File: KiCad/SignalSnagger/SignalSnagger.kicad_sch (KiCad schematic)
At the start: 81 parts, among them J101 Left, J102 Left, J103 Right, J104 Right, J105 36-5005-ND, J106 36-5006-ND, J107 36-5006-ND, J108 36-5005-ND, J909 36-5006-ND, J910 36-5006-ND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

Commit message: PCB Updates
31-Mar-2024
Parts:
- U102: value QS3253QG8 -> (none); footprint Package_SO:SSOP-16_3.9x4.9mm_P0.635mm -> (none)
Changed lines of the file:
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@@
       (effects (font (size 1.524 1.524) bold) (justify left))
     )
-    (property "Value" "QS3253QG8" (id 1) (at 210.82 45.72 0)
+    (property "Value" "" (id 1) (at 210.82 45.72 0)
       (effects (font (size 1.27 1.27) bold) (justify left))
     )
-    (property "Footprint" "Package_SO:SSOP-16_3.9x4.9mm_P0.635mm" (id 2) (at 199.39 54.61 0)
+    (property "Footprint" "" (id 2) (at 199.39 54.61 0)
       (effects (font (size 1.27 1.27)) hide)
     )
@@
     )
     (path "/2d0c2951-63ff-4560-b766-36e57ba946b0"
-      (reference "U102") (unit 1) (value "QS3253QG8") (footprint "Package_SO:SSOP-16_3.9x4.9mm_P0.635mm")
+      (reference "U102") (unit 1) (value "QS3253QG8") (footprint "Package_SO:SSOP-16_4.4x5.2mm_P0.65mm")
     )
     (path "/2fa45223-79ea-411b-839f-8bddbb1c8fec"

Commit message: Ver 0.315
BOM update
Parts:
- J102, J104: Digi-Key Part No. N/P -> SAM8996-ND; Manufacturer (none) -> Samtec Inc.; Manufacturer PN (none) -> TSW-104-07-F-D
- U102: value (none) -> QS3253QG8; footprint (none) -> Package_SO:SSOP-16_4.4x5.2mm_P0.65mm
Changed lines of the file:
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@@
   (title_block
     (title "SignalSnagger")
-    (date "2024-03-29")
-    (rev "0.314")
+    (date "2024-04-01")
+    (rev "0.315")
   )
   (junction (at 76.2 129.54) (diameter 0) (color 0 0 0 0)
@@
       (effects (font (size 1.524 1.524) bold) (justify left))
     )
-    (property "Value" "" (id 1) (at 210.82 45.72 0)
+    (property "Value" "QS3253QG8" (id 1) (at 210.82 45.72 0)
       (effects (font (size 1.27 1.27) bold) (justify left))
     )
-    (property "Footprint" "" (id 2) (at 199.39 54.61 0)
+    (property "Footprint" "Package_SO:SSOP-16_4.4x5.2mm_P0.65mm" (id 2) (at 199.39 54.61 0)
       (effects (font (size 1.27 1.27)) hide)
     )
@@
     (pin "1")
   )
-  (symbol (lib_id "Connector_Generic:Conn_02x04_Odd_Even") (at 68.58 92.71 0) (unit 1)
-    (in_bom yes) (on_board yes) (fields_autoplaced)
-    (property "Reference" "J104" (id 0) (at 69.85 85.2002 0))
-    (property "Value" "Right" (id 1) (at 69.85 87.7371 0))
-    (property "Footprint" "Connector_PinHeader_2.54mm:PinHeader_2x04_P2.54mm_Vertical" (id 2) (at 68.58 92.71 0)
-      (effects (font (size 1.27 1.27)) hide)
-    )
-    (property "Datasheet" "~" (id 3) (at 68.58 92.71 0)
-      (effects (font (size 1.27 1.27)) hide)
-    )
-    (property "Digi-Key Part No." "N/P" (id 4) (at 68.58 92.71 0)
-      (effects (font (size 1.27 1.27)) hide)
-    )
-    (pin "1")
-    (pin "2")
-    (pin "3")
-    (pin "4")
-    (pin "5")
-    (pin "6")
-    (pin "7")
-    (pin "8")
-  )
   (symbol (lib_id "Device:C_Trim_Small") (at 90.17 95.25 90) (mirror x) (unit 1)
     (in_bom yes) (on_board yes)
@@
       (effects (font (size 1.27 1.27)) hide)
     )
-    (property "Digi-Key Part No." "N/P" (id 4) (at 44.45 92.71 0)
+    (property "Digi-Key Part No." "SAM8996-ND" (id 4) (at 44.45 92.71 0)
+      (effects (font (size 1.27 1.27)) hide)
+    )
+    (property "Manufacturer" "Samtec Inc." (id 5) (at 44.45 92.71 0)
+      (effects (font (size 1.27 1.27)) hide)
+    )
+    (property "Manufacturer PN" "TSW-104-07-F-D" (id 6) (at 44.45 92.71 0)
+      (effects (font (size 1.27 1.27)) hide)
+    )
+    (property "Description" "CONN HEADER VERT 8POS 2.54MM" (id 7) (at 44.45 92.71 0)
       (effects (font (size 1.27 1.27)) hide)
     )
@@
     (pin "1")
   )
+  (symbol (lib_id "Connector_Generic:Conn_02x04_Odd_Even") (at 68.58 92.71 0) (unit 1)
+    (in_bom yes) (on_board yes) (fields_autoplaced)
+    (property "Reference" "J104" (id 0) (at 69.85 85.2002 0))
+    (property "Value" "Right" (id 1) (at 69.85 87.7371 0))
+    (property "Footprint" "Connector_PinHeader_2.54mm:PinHeader_2x04_P2.54mm_Vertical" (id 2) (at 68.58 92.71 0)
+      (effects (font (size 1.27 1.27)) hide)
+    )
+    (property "Datasheet" "~" (id 3) (at 68.58 92.71 0)
+      (effects (font (size 1.27 1.27)) hide)
+    )
+    (property "Digi-Key Part No." "SAM8996-ND" (id 4) (at 68.58 92.71 0)
+      (effects (font (size 1.27 1.27)) hide)
+    )
+    (property "Manufacturer" "Samtec Inc." (id 5) (at 68.58 92.71 0)
+      (effects (font (size 1.27 1.27)) hide)
+    )
+    (property "Manufacturer PN" "TSW-104-07-F-D" (id 6) (at 68.58 92.71 0)
+      (effects (font (size 1.27 1.27)) hide)
+    )
+    (property "Description" "CONN HEADER VERT 8POS 2.54MM" (id 7) (at 68.58 92.71 0)
+      (effects (font (size 1.27 1.27)) hide)
+    )
+    (pin "1")
+    (pin "2")
+    (pin "3")
+    (pin "4")
+    (pin "5")
+    (pin "6")
+    (pin "7")
+    (pin "8")
+  )
   (symbol (lib_id "Device:R_US") (at 139.7 180.34 0) (unit 1)
     (in_bom yes) (on_board yes)
@@
       (reference "J103") (unit 1) (value "Right") (footprint "Oddities:Dummy_Empty")
     )
-    (path "/331043fa-ab38-4872-afb0-dad5a0189da8"
+    (path "/edf6ad10-cc82-43d1-bc0a-205510d82ef2"
       (reference "J104") (unit 1) (value "Right") (footprint "Connector_PinHeader_2.54mm:PinHeader_2x04_P2.54mm_Vertical")
     )

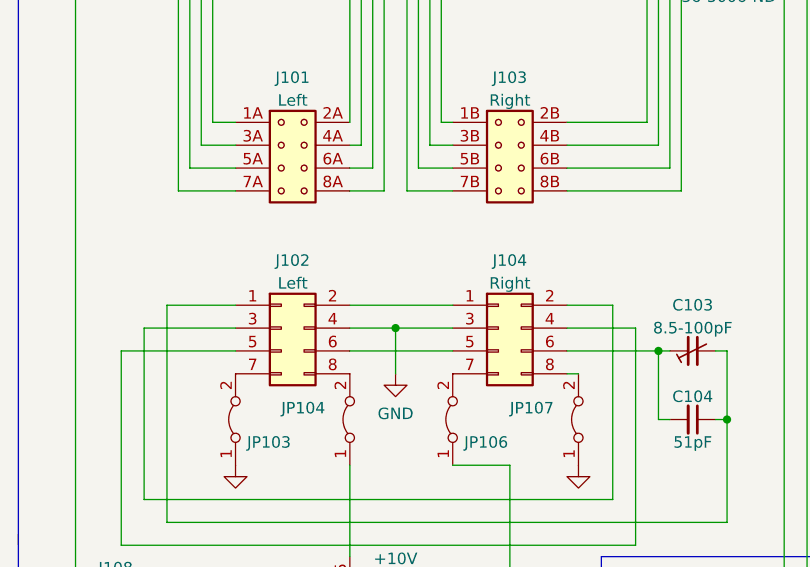
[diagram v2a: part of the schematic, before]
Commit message: PCB Updates
Moved programming header
Added ribbon cable plugs
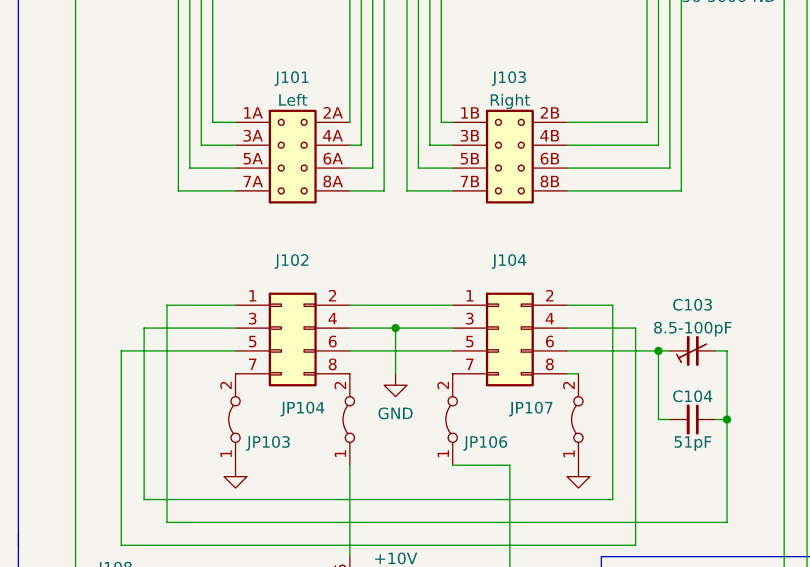
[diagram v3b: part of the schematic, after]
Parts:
- J102: value Left -> (none); footprint Connector_PinHeader_2.54mm:PinHeader_2x04_P2.54mm_Vertical -> (none); Digi-Key Part No. SAM8996-ND -> 609-3083-ND; Manufacturer Samtec Inc. -> Amphenol ICC (FCI); Manufacturer PN TSW-104-07-F-D -> 69830-008LF
- J104: value Right -> (none); footprint Connector_PinHeader_2.54mm:PinHeader_2x04_P2.54mm_Vertical -> (none); Digi-Key Part No. SAM8996-ND -> 609-3083-ND; Manufacturer Samtec Inc. -> Amphenol ICC (FCI); Manufacturer PN TSW-104-07-F-D -> 69830-008LF
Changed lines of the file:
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@@
     (pin "1")
+  )
+  (symbol (lib_id "Connector_Generic:Conn_02x04_Odd_Even") (at 68.58 92.71 0) (unit 1)
+    (in_bom yes) (on_board yes) (fields_autoplaced)
+    (property "Reference" "J104" (id 0) (at 69.85 85.2002 0))
+    (property "Value" "" (id 1) (at 69.85 87.7371 0))
+    (property "Footprint" "" (id 2) (at 68.58 92.71 0)
+      (effects (font (size 1.27 1.27)) hide)
+    )
+    (property "Datasheet" "~" (id 3) (at 68.58 92.71 0)
+      (effects (font (size 1.27 1.27)) hide)
+    )
+    (property "Digi-Key Part No." "609-3083-ND" (id 4) (at 68.58 92.71 0)
+      (effects (font (size 1.27 1.27)) hide)
+    )
+    (property "Manufacturer" "Amphenol ICC (FCI)" (id 5) (at 68.58 92.71 0)
+      (effects (font (size 1.27 1.27)) hide)
+    )
+    (property "Manufacturer PN" "69830-008LF" (id 6) (at 68.58 92.71 0)
+      (effects (font (size 1.27 1.27)) hide)
+    )
+    (property "Description" "CONN DIP HDR IDC 8POS VERT" (id 7) (at 68.58 92.71 0)
+      (effects (font (size 1.27 1.27)) hide)
+    )
+    (pin "1")
+    (pin "2")
+    (pin "3")
+    (pin "4")
+    (pin "5")
+    (pin "6")
+    (pin "7")
+    (pin "8")
   )
   (symbol (lib_id "Device:C_Small") (at 217.17 109.22 0) (unit 1)
@@
     (in_bom yes) (on_board yes) (fields_autoplaced)
     (property "Reference" "J102" (id 0) (at 45.72 85.2002 0))
-    (property "Value" "Left" (id 1) (at 45.72 87.7371 0))
-    (property "Footprint" "Connector_PinHeader_2.54mm:PinHeader_2x04_P2.54mm_Vertical" (id 2) (at 44.45 92.71 0)
+    (property "Value" "" (id 1) (at 45.72 87.7371 0))
+    (property "Footprint" "" (id 2) (at 44.45 92.71 0)
       (effects (font (size 1.27 1.27)) hide)
     )
@@
       (effects (font (size 1.27 1.27)) hide)
     )
-    (property "Digi-Key Part No." "SAM8996-ND" (id 4) (at 44.45 92.71 0)
-      (effects (font (size 1.27 1.27)) hide)
-    )
-    (property "Manufacturer" "Samtec Inc." (id 5) (at 44.45 92.71 0)
-      (effects (font (size 1.27 1.27)) hide)
-    )
-    (property "Manufacturer PN" "TSW-104-07-F-D" (id 6) (at 44.45 92.71 0)
-      (effects (font (size 1.27 1.27)) hide)
-    )
-    (property "Description" "CONN HEADER VERT 8POS 2.54MM" (id 7) (at 44.45 92.71 0)
+    (property "Digi-Key Part No." "609-3083-ND" (id 4) (at 44.45 92.71 0)
+      (effects (font (size 1.27 1.27)) hide)
+    )
+    (property "Manufacturer" "Amphenol ICC (FCI)" (id 5) (at 44.45 92.71 0)
+      (effects (font (size 1.27 1.27)) hide)
+    )
+    (property "Manufacturer PN" "69830-008LF" (id 6) (at 44.45 92.71 0)
+      (effects (font (size 1.27 1.27)) hide)
+    )
+    (property "Description" "CONN DIP HDR IDC 8POS VERT" (id 7) (at 44.45 92.71 0)
       (effects (font (size 1.27 1.27)) hide)
     )
@@
     (pin "1")
   )
-  (symbol (lib_id "Connector_Generic:Conn_02x04_Odd_Even") (at 68.58 92.71 0) (unit 1)
-    (in_bom yes) (on_board yes) (fields_autoplaced)
-    (property "Reference" "J104" (id 0) (at 69.85 85.2002 0))
-    (property "Value" "Right" (id 1) (at 69.85 87.7371 0))
-    (property "Footprint" "Connector_PinHeader_2.54mm:PinHeader_2x04_P2.54mm_Vertical" (id 2) (at 68.58 92.71 0)
-      (effects (font (size 1.27 1.27)) hide)
-    )
-    (property "Datasheet" "~" (id 3) (at 68.58 92.71 0)
-      (effects (font (size 1.27 1.27)) hide)
-    )
-    (property "Digi-Key Part No." "SAM8996-ND" (id 4) (at 68.58 92.71 0)
-      (effects (font (size 1.27 1.27)) hide)
-    )
-    (property "Manufacturer" "Samtec Inc." (id 5) (at 68.58 92.71 0)
-      (effects (font (size 1.27 1.27)) hide)
-    )
-    (property "Manufacturer PN" "TSW-104-07-F-D" (id 6) (at 68.58 92.71 0)
-      (effects (font (size 1.27 1.27)) hide)
-    )
-    (property "Description" "CONN HEADER VERT 8POS 2.54MM" (id 7) (at 68.58 92.71 0)
-      (effects (font (size 1.27 1.27)) hide)
-    )
-    (pin "1")
-    (pin "2")
-    (pin "3")
-    (pin "4")
-    (pin "5")
-    (pin "6")
-    (pin "7")
-    (pin "8")
-  )
   (symbol (lib_id "Device:R_US") (at 139.7 180.34 0) (unit 1)
     (in_bom yes) (on_board yes)
@@
     )
     (path "/90b403ba-135c-4ead-befc-3bc52036bd7e"
-      (reference "J102") (unit 1) (value "Left") (footprint "Connector_PinHeader_2.54mm:PinHeader_2x04_P2.54mm_Vertical")
+      (reference "J102") (unit 1) (value "Left") (footprint "Connector_Amphenol:69830-008LF")
     )
     (path "/b7c2c456-0540-49da-b4e7-60791f157ca9"
       (reference "J103") (unit 1) (value "Right") (footprint "Oddities:Dummy_Empty")
     )
-    (path "/edf6ad10-cc82-43d1-bc0a-205510d82ef2"
-      (reference "J104") (unit 1) (value "Right") (footprint "Connector_PinHeader_2.54mm:PinHeader_2x04_P2.54mm_Vertical")
+    (path "/8cd502e3-a78c-4b2f-8c7f-c0f8cafe4ad6"
+      (reference "J104") (unit 1) (value "Right") (footprint "Connector_Amphenol:69830-008LF")
     )
     (path "/1827fd48-a0ad-4504-ad60-021c20fdb5f0"

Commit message: PCB Layout
Most 3D models have been included in the schematic
PCB layout places all tall parts on the back of the board
Added knob to BOM
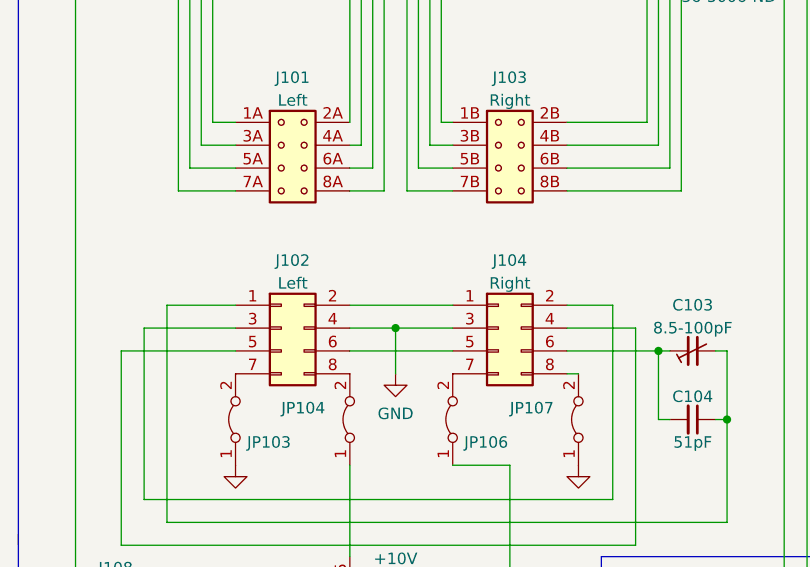
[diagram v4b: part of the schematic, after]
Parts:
- J102: value (none) -> Left; footprint (none) -> Connector_Amphenol:69830-008LF
- J104: value (none) -> Right; footprint (none) -> Connector_Amphenol:69830-008LF
- RV101: footprint Potentiometer_THT:Bourns_PV36W_Multiturn_Pot -> Potentiometer_THT:Potentiometer_Bourns_3362P_Vertical
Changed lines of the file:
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@@
   (title_block
     (title "SignalSnagger")
-    (date "2024-04-01")
-    (rev "0.315")
+    (date "2024-04-11")
+    (rev "0.316")
   )
   (junction (at 76.2 129.54) (diameter 0) (color 0 0 0 0)
@@
     (in_bom yes) (on_board yes) (fields_autoplaced)
     (property "Reference" "J104" (id 0) (at 69.85 85.2002 0))
-    (property "Value" "" (id 1) (at 69.85 87.7371 0))
-    (property "Footprint" "" (id 2) (at 68.58 92.71 0)
+    (property "Value" "Right" (id 1) (at 69.85 87.7371 0))
+    (property "Footprint" "Connector_Amphenol:69830-008LF" (id 2) (at 68.58 92.71 0)
       (effects (font (size 1.27 1.27)) hide)
     )
@@
     (in_bom yes) (on_board yes) (fields_autoplaced)
     (property "Reference" "J102" (id 0) (at 45.72 85.2002 0))
-    (property "Value" "" (id 1) (at 45.72 87.7371 0))
-    (property "Footprint" "" (id 2) (at 44.45 92.71 0)
+    (property "Value" "Left" (id 1) (at 45.72 87.7371 0))
+    (property "Footprint" "Connector_Amphenol:69830-008LF" (id 2) (at 44.45 92.71 0)
       (effects (font (size 1.27 1.27)) hide)
     )
@@
     (property "Reference" "RV101" (id 0) (at 33.02 133.35 90))
     (property "Value" "10k 10T" (id 1) (at 36.83 140.97 90))
-    (property "Footprint" "Potentiometer_THT:Bourns_PV36W_Multiturn_Pot" (id 2) (at 34.29 140.97 0)
+    (property "Footprint" "Potentiometer_THT:Potentiometer_Bourns_3362P_Vertical" (id 2) (at 34.29 140.97 0)
       (effects (font (size 1.27 1.27)) hide)
     )
@@
       (reference "JP301") (unit 1) (value "SolderJumper_2_Open") (footprint "Jumper:SolderJumper-2_P1.3mm_Open_RoundedPad1.0x1.5mm")
     )
+    (path "/a07b7207-b2ba-4964-b1bd-fe9eb7be7391/3433a5ee-7118-4568-bf67-046adea068c5"
+      (reference "Knob401") (unit 1) (value "Logo_Open_Hardware_Small") (footprint "")
+    )
     (path "/b7e6c0d8-791a-469a-85d5-f8e886443224/baca905f-d9c0-4905-a617-69cf46299e1f"
       (reference "L201") (unit 1) (value "10uH") (footprint "Inductor_SMD:L_0603_1608Metric")
@@
     )
     (path "/c0687338-f6ed-4456-aad9-d29c3bd35909"
-      (reference "RV101") (unit 1) (value "10k 10T") (footprint "Potentiometer_THT:Bourns_PV36W_Multiturn_Pot")
+      (reference "RV101") (unit 1) (value "10k 10T") (footprint "Potentiometer_THT:Potentiometer_Bourns_3362P_Vertical")
     )
     (path "/22206298-fd84-4e61-b115-2fa251b44661"

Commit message: Ver 0.317
PCB Tweaks
FreeCAD model updates
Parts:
- RV101: Digi-Key Part No. 118-PV36W103C01B00-ND -> 3362P-103LF-ND; Link https://www.digikey.com/en/products/detail/bourns-inc/PV36W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 -> https://www.digikey.com/en/products/detail/bourns-inc/3362P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; Manufacturer PN PV36W103C01B00 -> 3362P-1-103LF
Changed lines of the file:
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@@
   (title_block
     (title "SignalSnagger")
-    (date "2024-04-11")
-    (rev "0.316")
+    (date "2024-04-13")
+    (rev "0.317")
   )
   (junction (at 76.2 129.54) (diameter 0) (color 0 0 0 0)
@@
       (effects (font (size 1.27 1.27)) hide)
     )
-    (property "Digi-Key Part No." "118-PV36W103C01B00-ND" (id 4) (at 34.29 140.97 0)
+    (property "Digi-Key Part No." "3362P-103LF-ND" (id 4) (at 34.29 140.97 0)
       (effects (font (size 1.27 1.27)) hide)
     )
-    (property "Link" "https://www.digikey.com/en/products/detail/bourns-inc/PV36W103C01B00/666502?s=N4IgTCBcDaIAoDUDMA2A6gRgAxIMJYwCEssQBdAXyA" (id 5) (at 34.29 140.97 0)
+    (property "Link" "https://www.digikey.com/en/products/detail/bourns-inc/3362P-1-103LF/1088412?s=N4IgTCBcDaIMxwGxgAoFoCMAGOAZAYmgHIAiIAugL5A" (id 5) (at 34.29 140.97 0)
       (effects (font (size 1.27 1.27)) hide)
     )
@@
       (effects (font (size 1.27 1.27)) hide)
     )
-    (property "Manufacturer PN" "PV36W103C01B00" (id 7) (at 34.29 140.97 0)
+    (property "Manufacturer PN" "3362P-1-103LF" (id 7) (at 34.29 140.97 0)
       (effects (font (size 1.27 1.27)) hide)
     )
-    (property "Description" "10 kOhms 0.5W, 1/2W PC Pins Through Hole Trimmer Potentiometer Cermet 25 Turn Top Adjustment" (id 8) (at 34.29 140.97 0)
+    (property "Description" "TRIMMER 10K OHM 0.5W PC PIN TOP" (id 8) (at 34.29 140.97 0)
       (effects (font (size 1.27 1.27)) hide)
     )

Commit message: BOM Updates
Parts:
- J102: value Left -> (none); footprint Connector_Amphenol:69830-008LF -> (none)
- J104: value Right -> (none); footprint Connector_Amphenol:69830-008LF -> (none)
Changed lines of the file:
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@@
-    (pin "1")
-  )
-  (symbol (lib_id "Connector_Generic:Conn_01x01") (at 96.52 52.07 0) (unit 1)
-    (in_bom yes) (on_board yes)
-    (property "Reference" "J106" (id 0) (at 95.25 49.53 0)
-      (effects (font (size 1.27 1.27)) (justify left))
-    )
-    (property "Value" "36-5006-ND" (id 1) (at 88.9 55.88 0)
-      (effects (font (size 1.27 1.27)) (justify left))
-    )
-    (property "Footprint" "Connector_Pin:Pin_D1.6mm_L8.5mm_W2.8mm_FlatFork" (id 2) (at 96.52 52.07 0)
-      (effects (font (size 1.27 1.27)) hide)
-    )
-    (property "Datasheet" "~" (id 3) (at 96.52 52.07 0)
-      (effects (font (size 1.27 1.27)) hide)
-    )
-    (property "Digi-Key Part No." "N/P" (id 4) (at 96.52 52.07 0)
-      (effects (font (size 1.27 1.27)) hide)
-    )
     (pin "1")
   )
   (symbol (lib_id "Connector_Generic:Conn_02x04_Odd_Even") (at 68.58 92.71 0) (unit 1)
     (in_bom yes) (on_board yes) (fields_autoplaced)
-    (property "Reference" "J104" (id 0) (at 69.85 85.2002 0))
-    (property "Value" "Right" (id 1) (at 69.85 87.7371 0))
-    (property "Footprint" "Connector_Amphenol:69830-008LF" (id 2) (at 68.58 92.71 0)
+    (property "Reference" "J104" (id 0) (at 69.85 87.7372 0))
+    (property "Value" "" (id 1) (at 69.85 87.7371 0)
+      (effects (font (size 1.27 1.27)) hide)
+    )
+    (property "Footprint" "" (id 2) (at 68.58 92.71 0)
       (effects (font (size 1.27 1.27)) hide)
     )
@@
     (pin "8")
   )
+  (symbol (lib_id "Connector_Generic:Conn_01x01") (at 96.52 52.07 0) (unit 1)
+    (in_bom yes) (on_board yes)
+    (property "Reference" "J106" (id 0) (at 95.25 49.53 0)
+      (effects (font (size 1.27 1.27)) (justify left))
+    )
+    (property "Value" "36-5006-ND" (id 1) (at 88.9 55.88 0)
+      (effects (font (size 1.27 1.27)) (justify left))
+    )
+    (property "Footprint" "Connector_Pin:Pin_D1.6mm_L8.5mm_W2.8mm_FlatFork" (id 2) (at 96.52 52.07 0)
+      (effects (font (size 1.27 1.27)) hide)
+    )
+    (property "Datasheet" "~" (id 3) (at 96.52 52.07 0)
+      (effects (font (size 1.27 1.27)) hide)
+    )
+    (property "Digi-Key Part No." "N/P" (id 4) (at 96.52 52.07 0)
+      (effects (font (size 1.27 1.27)) hide)
+    )
+    (pin "1")
+  )
   (symbol (lib_id "Device:C_Small") (at 217.17 109.22 0) (unit 1)
     (in_bom yes) (on_board yes)
@@
   (symbol (lib_id "Connector_Generic:Conn_02x04_Odd_Even") (at 44.45 92.71 0) (unit 1)
     (in_bom yes) (on_board yes) (fields_autoplaced)
-    (property "Reference" "J102" (id 0) (at 45.72 85.2002 0))
-    (property "Value" "Left" (id 1) (at 45.72 87.7371 0))
-    (property "Footprint" "Connector_Amphenol:69830-008LF" (id 2) (at 44.45 92.71 0)
+    (property "Reference" "J102" (id 0) (at 45.72 87.7372 0))
+    (property "Value" "" (id 1) (at 45.72 87.7371 0)
+      (effects (font (size 1.27 1.27)) hide)
+    )
+    (property "Footprint" "" (id 2) (at 44.45 92.71 0)
       (effects (font (size 1.27 1.27)) hide)
     )
@@
     )
     (path "/90b403ba-135c-4ead-befc-3bc52036bd7e"
-      (reference "J102") (unit 1) (value "Left") (footprint "Connector_Amphenol:69830-008LF")
+      (reference "J102") (unit 1) (value "69830-008LF") (footprint "Connector_Amphenol:69830-008LF")
     )
     (path "/b7c2c456-0540-49da-b4e7-60791f157ca9"
       (reference "J103") (unit 1) (value "Right") (footprint "Oddities:Dummy_Empty")
     )
-    (path "/8cd502e3-a78c-4b2f-8c7f-c0f8cafe4ad6"
-      (reference "J104") (unit 1) (value "Right") (footprint "Connector_Amphenol:69830-008LF")
+    (path "/8a0e5179-fef2-43e1-bcf9-390e85dd7c99"
+      (reference "J104") (unit 1) (value "69830-008LF") (footprint "Connector_Amphenol:69830-008LF")
     )
     (path "/1827fd48-a0ad-4504-ad60-021c20fdb5f0"
@@
       (reference "U205") (unit 1) (value "EA_DOGS104W-A") (footprint "Display:EA_DOGS104X-A")
     )
-    (path "/b7e6c0d8-791a-469a-85d5-f8e886443224/c2f4c89a-a957-4b76-822b-6a2541c0d249"
+    (path "/b7e6c0d8-791a-469a-85d5-f8e886443224/8eb6d55e-a524-4dfa-9f3c-f6e2b6c699d3"
       (reference "U206") (unit 1) (value "LP2985-5.0") (footprint "Package_TO_SOT_SMD:SOT-23-5")
     )
